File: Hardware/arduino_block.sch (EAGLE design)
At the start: 37 parts, among them U1 MIC5205-3.3V (150mA), U2 EDISON_CONNECTOR_FULLMOUNTING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, U3 EDISON_CONNECTOR_FULLHEADER, U4 ATMEGA328, Y1 8MHZ

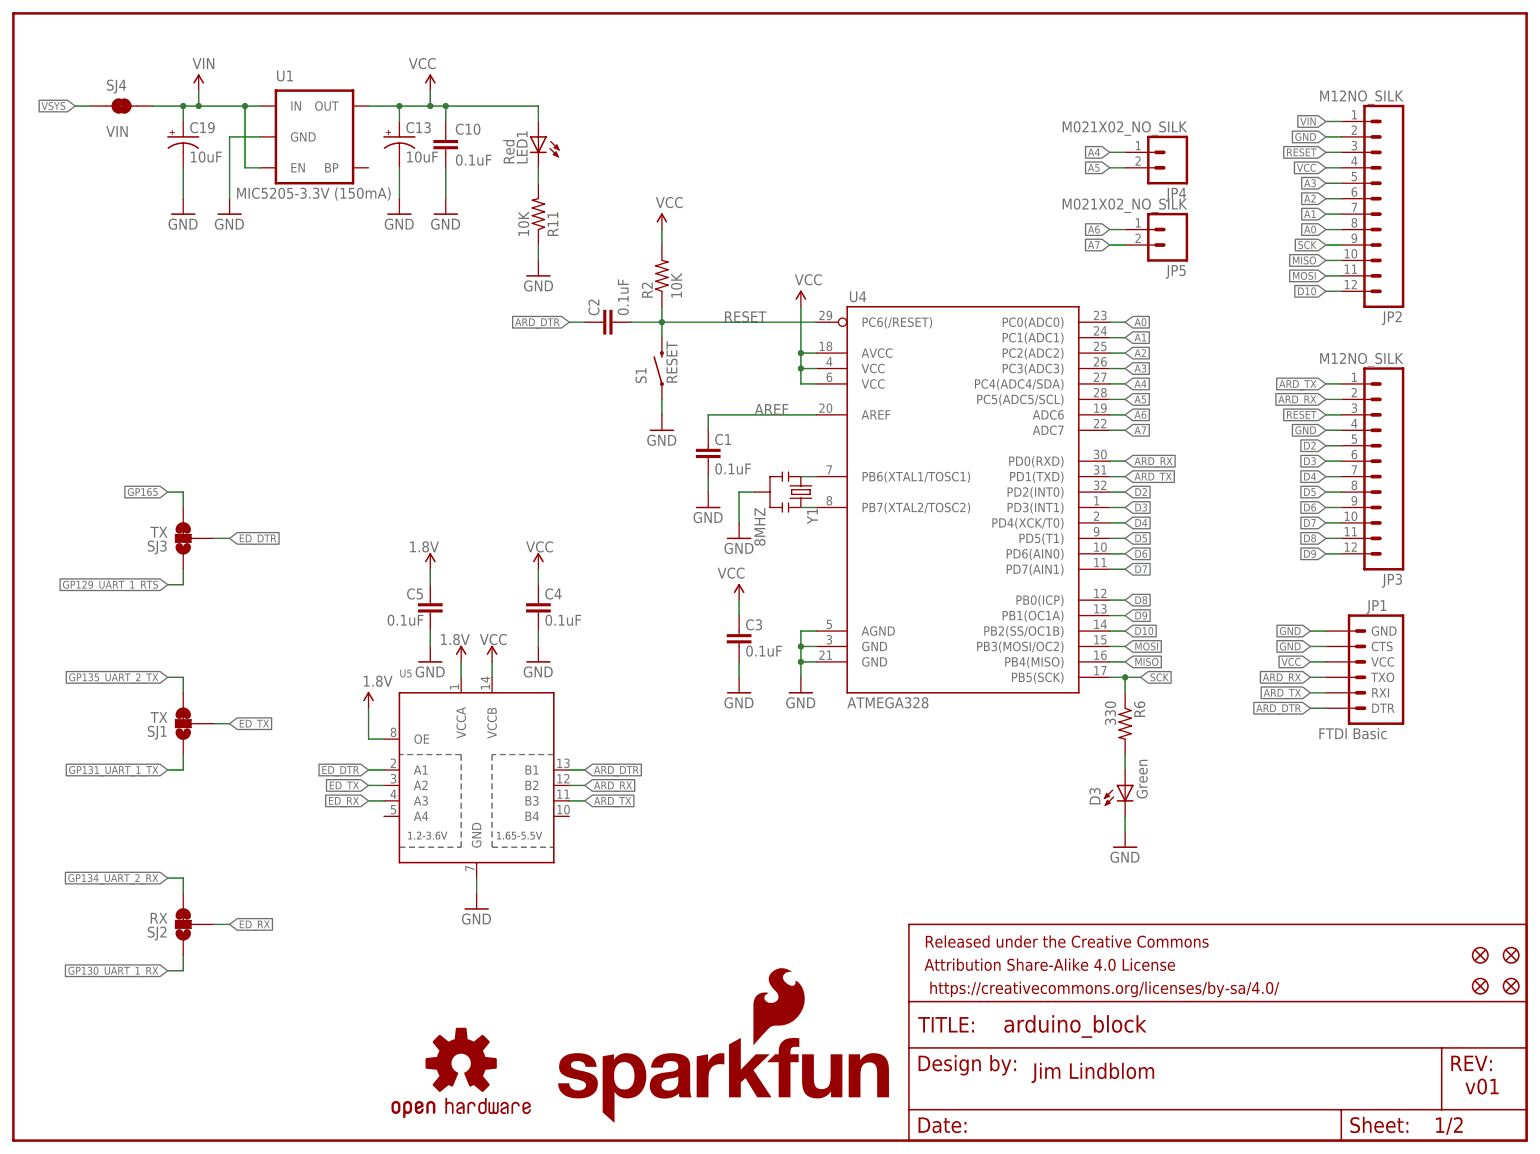
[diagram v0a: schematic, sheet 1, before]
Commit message: Swapping jumpers to default to UART 1. Updating silk. (v02)
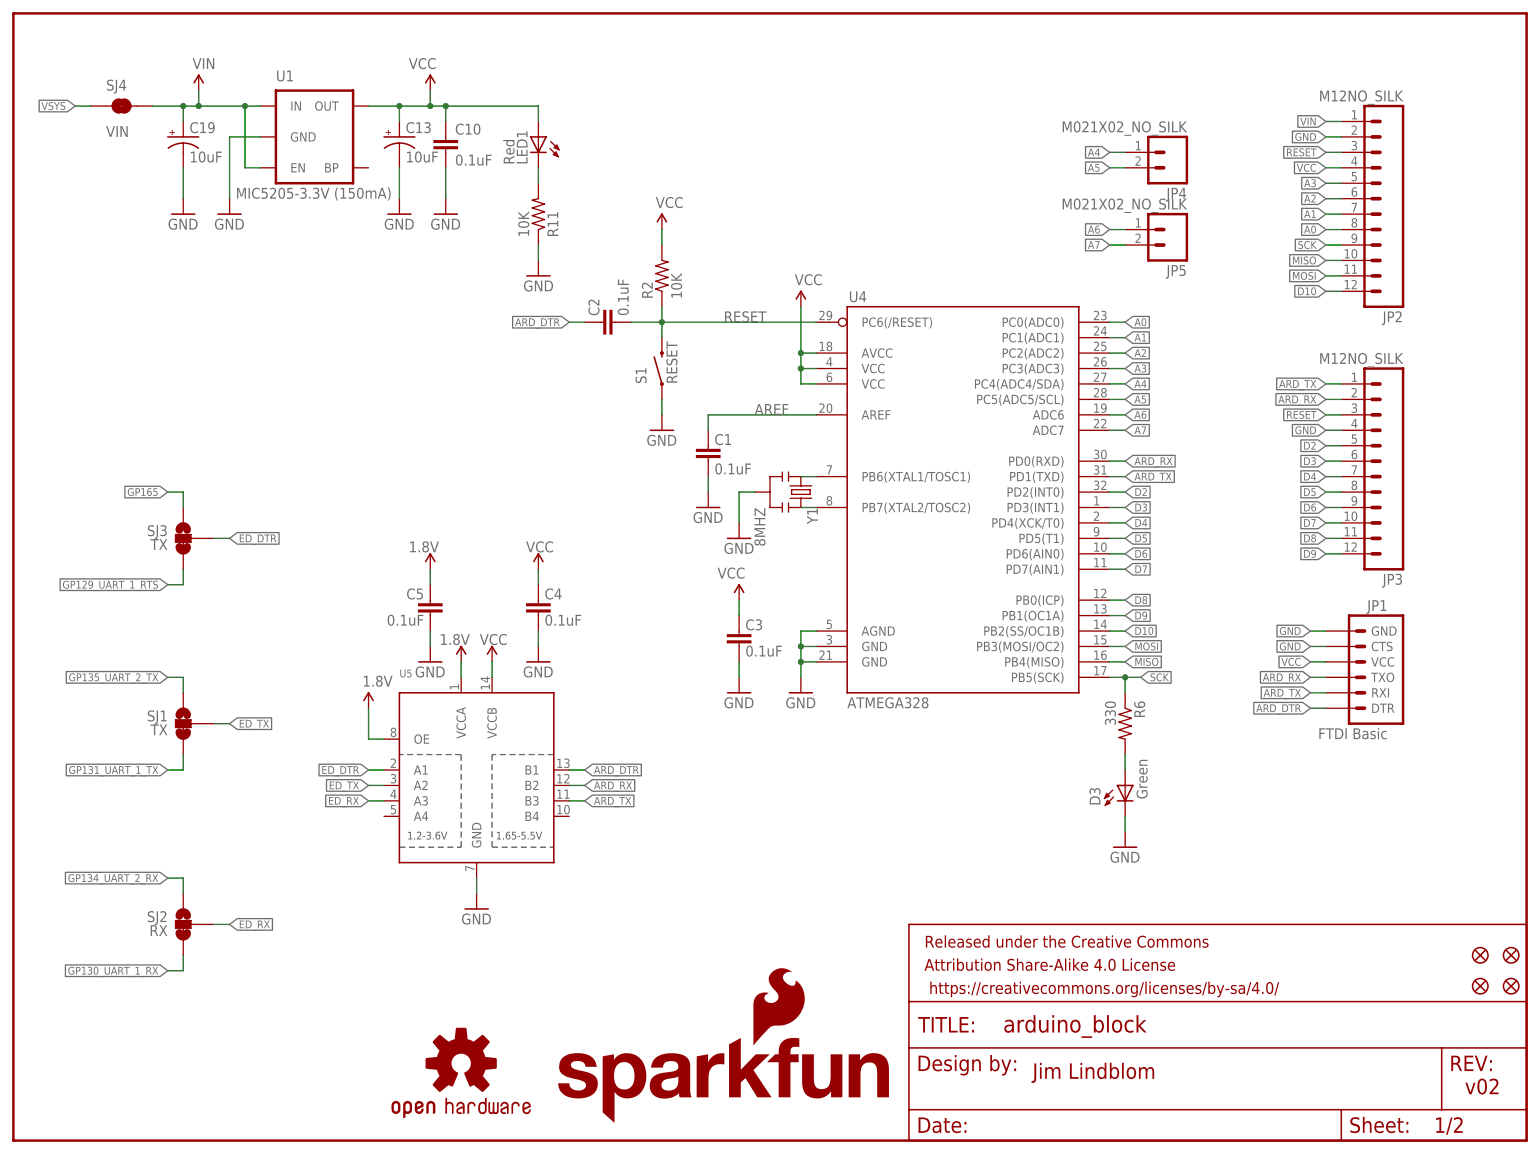
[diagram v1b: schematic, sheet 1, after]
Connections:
- net GP129_UART_1_RTS: now also SJ3.3; no longer SJ3.1
- net GP130_UART_1_RX: now also SJ2.3; no longer SJ2.1
- net GP131_UART_1_TX: now also SJ1.3; no longer SJ1.1
- net GP134_UART_2_RX: now also SJ2.1; no longer SJ2.3
- net GP135_UART_2_TX: now also SJ1.1; no longer SJ1.3
- net GP165: now also SJ3.1; no longer SJ3.3
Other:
- note added: "v02"
- note removed: "v01"
- moved on the sheet: SJ1, SJ2, SJ3

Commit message: Stacking DCIN through. Adding jumper to potentially connect it to VSYS
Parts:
- added SJ5: DCIN, SparkFun-Passives:JUMPER-PAD-2-NOYES_SILK
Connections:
- new net DCIN: SJ5.1, U2.DCIN, U3.DCIN
- net VSYS: now also SJ5.2
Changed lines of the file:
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@@
 <part name="JP4" library="SparkFun-Connectors" deviceset="M02" device="1X02_NO_SILK" value="M021X02_NO_SILK"/>
 <part name="JP5" library="SparkFun-Connectors" deviceset="M02" device="1X02_NO_SILK" value="M021X02_NO_SILK"/>
+<part name="SJ5" library="SparkFun-Passives" deviceset="JUMPER-PAD-2-NO" device="YES_SILK" value="DCIN"/>
 </parts>
 <sheets>
@@
 <instance part="JP4" gate="G$1" x="190.5" y="162.56" rot="R180"/>
 <instance part="JP5" gate="G$1" x="190.5" y="149.86" rot="R180"/>
+<instance part="SJ5" gate="G$1" x="27.94" y="15.24"/>
 </instances>
 <busses>
@@
 <label x="10.16" y="170.18" size="1.27" layer="95" rot="R180" xref="yes"/>
 </segment>
+<segment>
+<pinref part="SJ5" gate="G$1" pin="2"/>
+<wire x1="33.02" y1="15.24" x2="35.56" y2="15.24" width="0.1524" layer="91"/>
+<label x="35.56" y="15.24" size="1.27" layer="95" xref="yes"/>
+</segment>
 </net>
 <net name="GP135_UART_2_TX" class="0">
@@
 <pinref part="SUPPLY3" gate="G$1" pin="1.8V"/>
 <wire x1="68.58" y1="93.98" x2="68.58" y2="91.44" width="0.1524" layer="91"/>
+</segment>
+</net>
+<net name="DCIN" class="0">
+<segment>
+<pinref part="SJ5" gate="G$1" pin="1"/>
+<wire x1="22.86" y1="15.24" x2="20.32" y2="15.24" width="0.1524" layer="91"/>
+<label x="20.32" y="15.24" size="1.27" layer="95" rot="R180" xref="yes"/>
 </segment>
 </net>
@@
 </segment>
 </net>
+<net name="DCIN" class="0">
+<segment>
+<pinref part="U2" gate="G$1" pin="DCIN"/>
+<wire x1="25.4" y1="152.4" x2="20.32" y2="152.4" width="0.1524" layer="91"/>
+<label x="20.32" y="152.4" size="1.27" layer="95" rot="R180" xref="yes"/>
+</segment>
+<segment>
+<pinref part="U3" gate="G$1" pin="DCIN"/>
+<wire x1="172.72" y1="152.4" x2="167.64" y2="152.4" width="0.1524" layer="91"/>
+<label x="167.64" y="152.4" size="1.27" layer="95" rot="R180" xref="yes"/>
+</segment>
+</net>

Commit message: Replaced reset button with new RA SMD push button
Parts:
- S1: device SparkFun-Electromechanical:SWITCH-MOMENTARY-2-SMD-1101NE -> SparkFun-Electromechanical:SWITCH-MOMENTARY-2TACTILE-SWITCH-SMD-RIGHT-ANGLE
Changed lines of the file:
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@@
 <?xml version="1.0" encoding="utf-8"?>
 <!DOCTYPE eagle SYSTEM "eagle.dtd">
-<eagle version="7.1.0">
+<eagle version="6.5.0">
 <drawing>
 <settings>
@@
 <part name="JP1" library="SparkFun" deviceset="ARDUINO_SERIAL_PROGRAM" device="PTH" value="FTDI Basic"/>
 <part name="C2" library="SparkFun" deviceset="CAP" device="0603-CAP" value="0.1uF"/>
-<part name="S1" library="SparkFun-Electromechanical" deviceset="SWITCH-MOMENTARY-2" device="-SMD-1101NE" value="RESET"/>
 <part name="Y1" library="SparkFun-FreqCtrl" deviceset="RESONATOR" device="8MHZ" value="8MHZ"/>
 <part name="SJ1" library="SparkFun-Passives" deviceset="JUMPER-PAD-3-2OF3_NC_BY_TRACE" device="" value="TX"/>
@@
 <part name="JP5" library="SparkFun-Connectors" deviceset="M02" device="1X02_NO_SILK" value="M021X02_NO_SILK"/>
 <part name="SJ5" library="SparkFun-Passives" deviceset="JUMPER-PAD-2-NO" device="YES_SILK" value="DCIN"/>
+<part name="S1" library="SparkFun-Electromechanical" deviceset="SWITCH-MOMENTARY-2" device="TACTILE-SWITCH-SMD-RIGHT-ANGLE" value="RESET"/>
 </parts>
 <sheets>
@@
 <attribute name="VALUE" x="101.219" y="135.636" size="1.778" layer="96" rot="R90"/>
 </instance>
-<instance part="S1" gate="G$1" x="106.68" y="127" rot="R90"/>
 <instance part="Y1" gate="G$1" x="129.54" y="106.68" rot="R270"/>
 <instance part="SJ1" gate="G$1" x="27.94" y="68.58" rot="MR0"/>
@@
 <instance part="JP5" gate="G$1" x="190.5" y="149.86" rot="R180"/>
 <instance part="SJ5" gate="G$1" x="27.94" y="15.24"/>
+<instance part="S1" gate="G$1" x="106.68" y="127" rot="R90"/>
 </instances>
 <busses>

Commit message: updating connector packages. Fixing silk.
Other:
- note added: "v10"
- note removed: "v02"
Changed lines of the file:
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@@
 <?xml version="1.0" encoding="utf-8"?>
 <!DOCTYPE eagle SYSTEM "eagle.dtd">
-<eagle version="6.5.0">
+<eagle version="7.1.0">
 <drawing>
 <settings>
@@
 <sheet>
 <plain>
-<text x="238.76" y="7.62" size="2.54" layer="94">v02</text>
+<text x="238.76" y="7.62" size="2.54" layer="94">v10</text>
 <text x="167.64" y="10.16" size="2.54" layer="94">Jim Lindblom</text>
 </plain>
